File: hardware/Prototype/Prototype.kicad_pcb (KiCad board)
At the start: 2 copper layers, 53.3 x 63.5 mm, 3 parts, among them U1 Adafruit_24_TFT, U2 Adafruit_ItsyBitsy_M0, U3 Adafruit_MAX31855

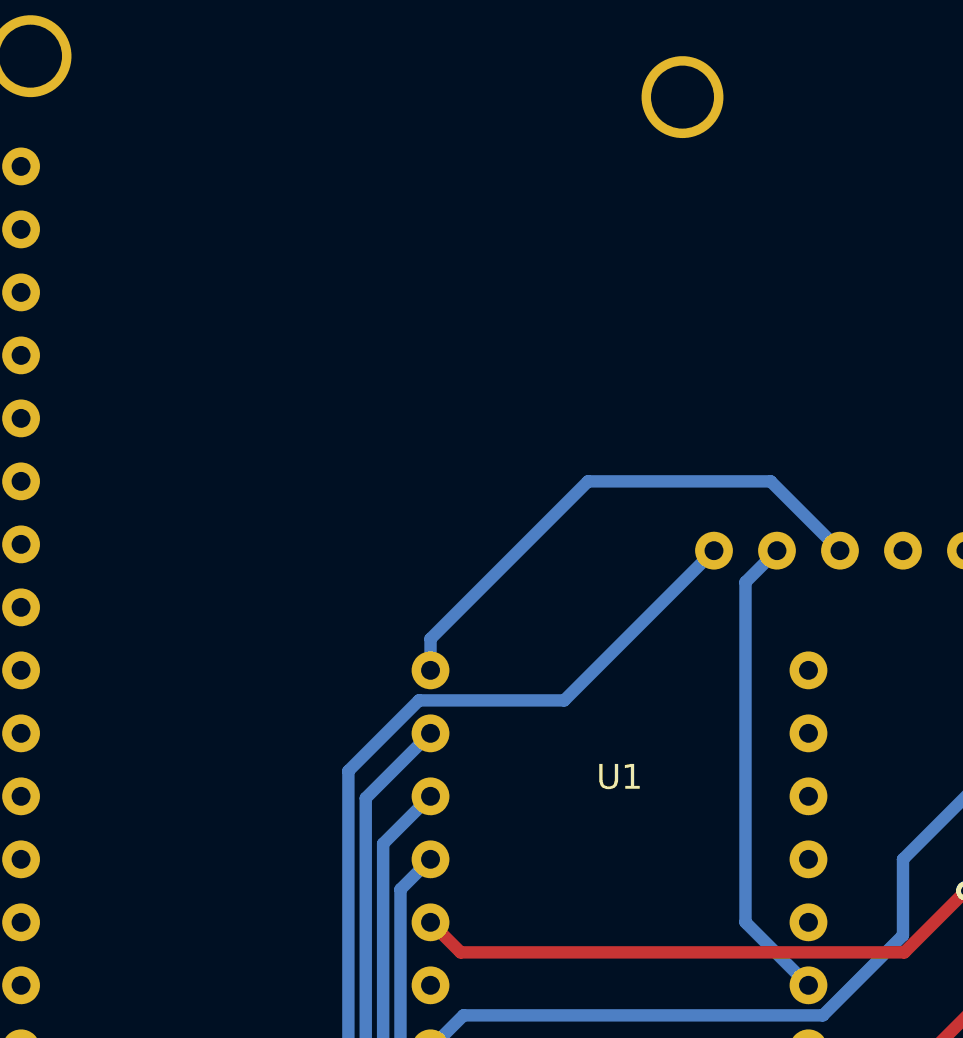
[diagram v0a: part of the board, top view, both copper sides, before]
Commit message: Add SSR connector to controller board
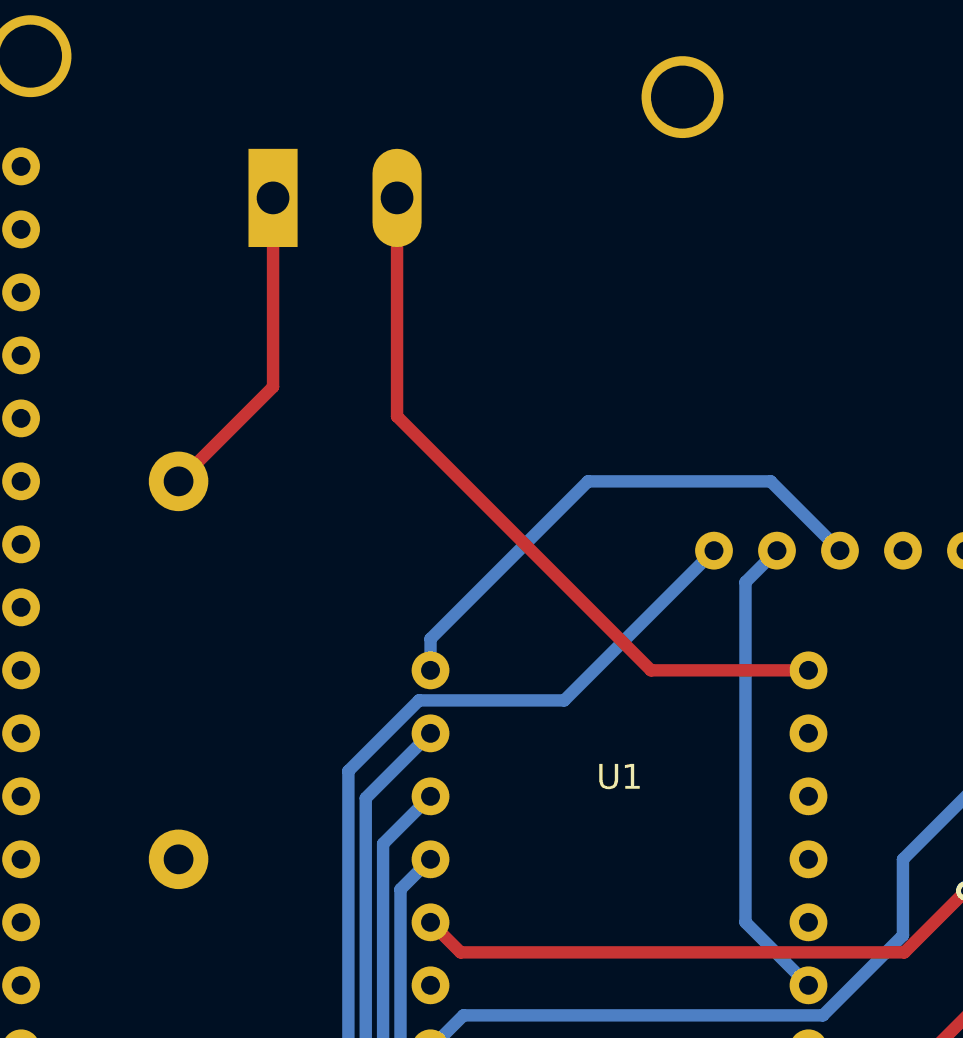
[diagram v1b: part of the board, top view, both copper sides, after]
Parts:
- added J1: Screw_Terminal_01x02, TerminalBlock:TerminalBlock_Altech_AK300-2_P5.00mm, B.Cu at (135.9, 71.1)
- added R1: 10k, Resistor_THT:R_Axial_DIN0411_L9.9mm_D3.6mm_P15.24mm_Horizontal, B.Cu at (132.1, 82.5)
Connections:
- U2 pad 1: Net-(U2-Pad1) -> SSR_EN
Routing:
- net SSR_EN: track 0.00 -> 29.6 mm
- net Net-(J1-Pad1): track 0.00 -> 13.0 mm
